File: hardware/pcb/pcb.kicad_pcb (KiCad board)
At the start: 4 copper layers, 41.5 x 66.5 mm, 157 parts, among them J300 Conn_01x02, J301 AudioJack3_Ground_SwitchTR, J400 Conn_02x10_Top_Bottom_Mountin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, J700 USB_B_Micro, U1 AXP209, U101 W25Q32JVZP, U2 SY8008, U300 WM8960, U401 TPS65631W, U402 AP2127K-3.0, U700 USBLC6-2SC6, X100 24.576MHz

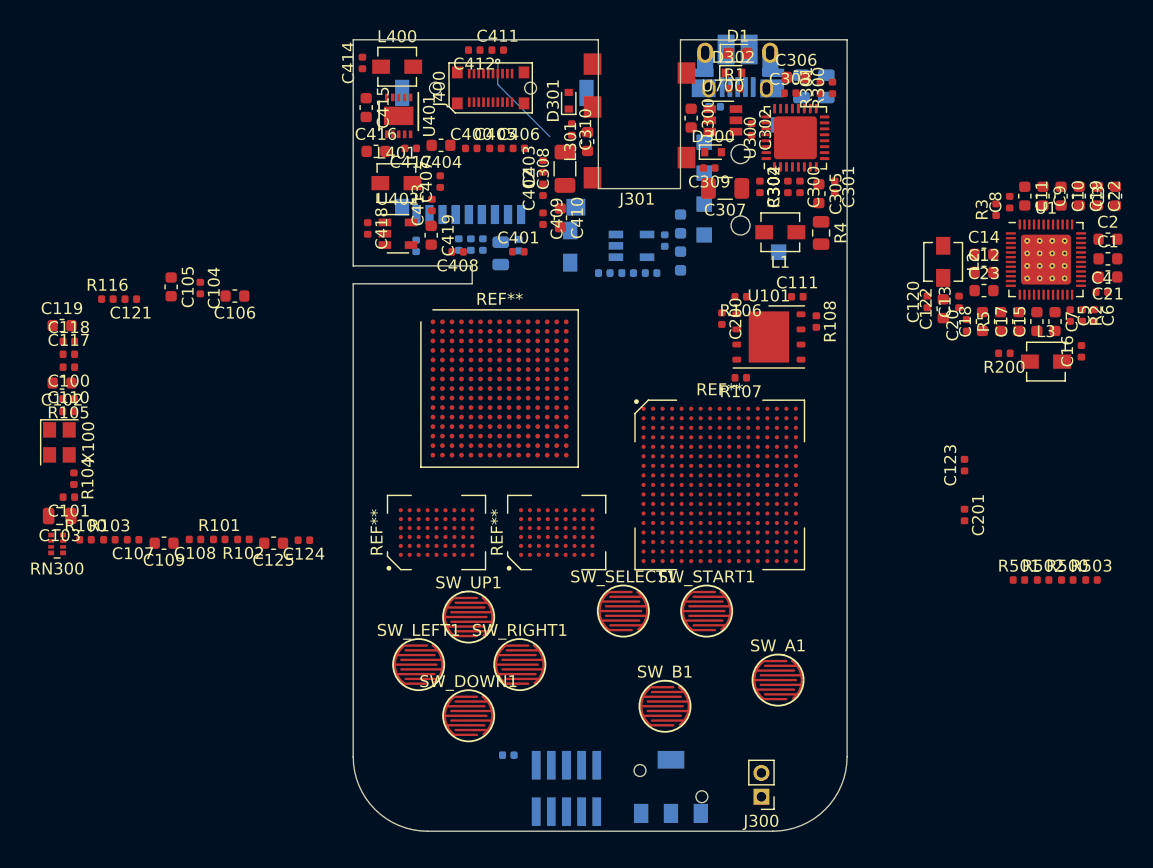
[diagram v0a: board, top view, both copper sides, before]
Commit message: - Migrate to KiCAD 5.99 nightly, pcb initial layout
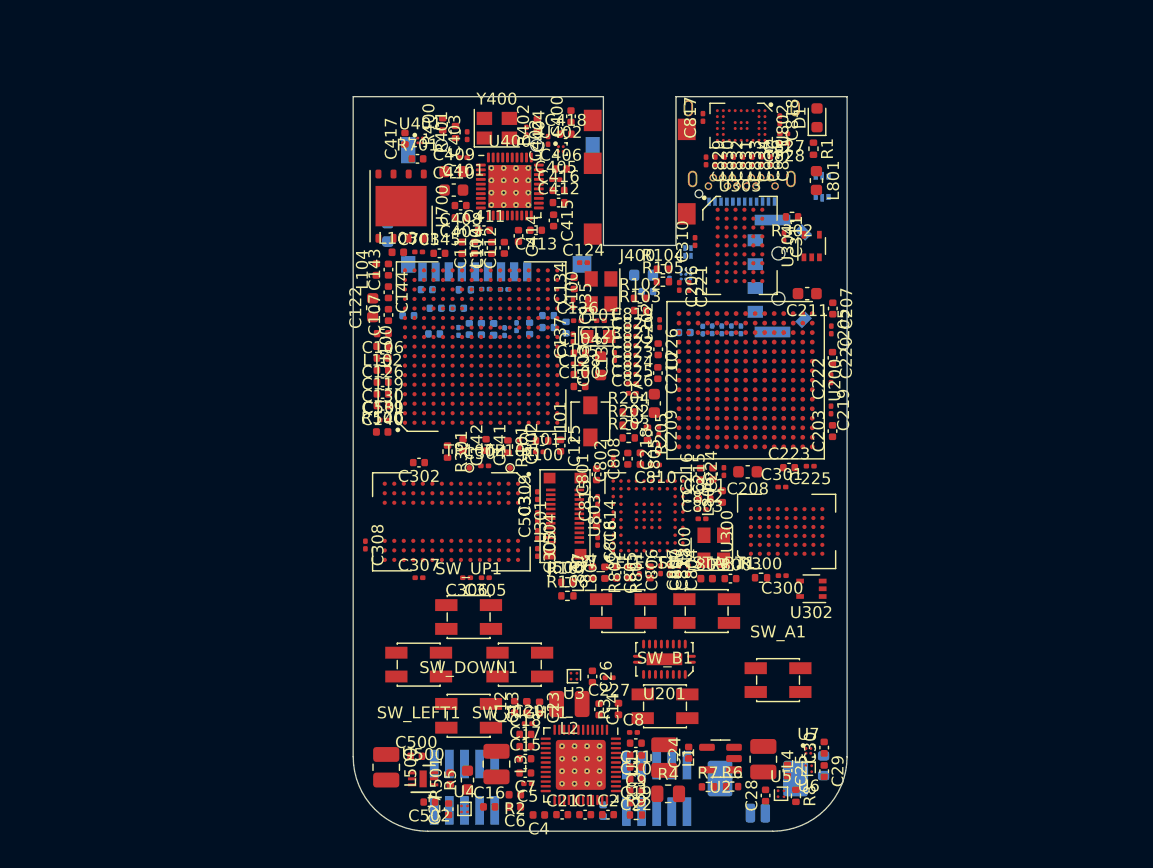
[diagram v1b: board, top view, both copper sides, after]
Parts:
- removed BAT1: Conn_01x03, footprint:BC-15-3P
- removed C419: 4.7uF, Capacitor_SMD:C_0603_1608Metric
- removed C600: 18pF, Capacitor_SMD:C_0402_1005Metric
- removed C601: 47uF, Capacitor_SMD:C_0805_2012Metric
- removed C602: 100nF, Capacitor_SMD:C_0402_1005Metric
- removed D300, D301, D302: ESD5B5.0ST1G, Diode_SMD:D_SOD-523
- removed D700: B72590D0050H160, Diode_SMD:D_0402_1005Metric
- removed ENC1: SIQ-02FVS3, footprint:SIQ-02FVS3
- removed FPGA_JTAG1: Conn_02x05_Odd_Even, Connector_PinHeader_1.27mm:PinHeader_2x05_P1.27mm_Vertical_SMD
- removed J300: Conn_01x02, Connector_PinHeader_2.00mm:PinHeader_1x02_P2.00mm_Vertical
- removed J301: AudioJack3_Ground_SwitchTR, footprint:PJ-327E
- removed J700: USB_B_Micro, Connector_USB:USB_Micro-B_Amphenol_10103594-0001LF_Horizontal
- removed L300, L301: BLM18BD252SN1, Inductor_SMD:L_0603_1608Metric
- removed L400, L401: 10uH, Inductor_SMD:L_Vishay_IHLP-1212
- removed MICRO_SD300: MICRO_SD(TFC-WPAPR-08), footprint:TFC-WPAPR-08
- removed R108: 100K, Capacitor_SMD:C_0402_1005Metric
- removed R116: 2.2K, Capacitor_SMD:C_0402_1005Metric
- removed R117: 4.7K, Capacitor_SMD:C_0402_1005Metric
- removed R502, R503, R601, R602: 10K, Resistor_SMD:R_0402_1005Metric
- removed R600: 33R, Resistor_SMD:R_0402_1005Metric
- removed REF** (x2): BGA-54_6x9_6.0x8.0mm, footprint:BGA-54_6x9_6.0x8.0mm
- removed REF**: BGA-289_17x17_14.0x14.0mm, footprint:BGA-289_17x17_14.0x14.0mm
- removed REF**: Xilinx_CSGA225, Package_BGA:Xilinx_CSGA225
- removed RN300: 22, Resistor_SMD:R_Array_Convex_4x0402
- removed U101: W25Q32JVZP, Package_SON:WSON-8-1EP_6x5mm_P1.27mm_EP3.4x4.3mm
- removed X100: 24.576MHz, Oscillator:Oscillator_SMD_Abracon_ASE-4Pin_3.2x2.5mm
- added BT1: Conn_01x02, Connector_Molex:Molex_PicoBlade_53261-0271_1x02-1MP_P1.25mm_Horizontal, B.Cu at (134.0, 112.6)
- added C112: 1uF, Capacitor_SMD:C_0402_1005Metric, F.Cu at (112.7, 67.5)
- added C113: 2.2uF, Capacitor_SMD:C_0402_1005Metric, F.Cu at (110.2, 67.5)
- added C114: 1uF, Capacitor_SMD:C_0402_1005Metric, F.Cu at (111.6, 67.5)
- added C115: 100nF, Capacitor_SMD:C_0201_0603Metric, B.Cu at (113.7, 74.1)
- added C116: 2.2uF, Capacitor_SMD:C_0402_1005Metric, B.Cu at (114.8, 74.2)
- added C126: 1uF, Capacitor_SMD:C_0402_1005Metric, F.Cu at (102.5, 76.8)
- added C127: 1uF, Capacitor_SMD:C_0402_1005Metric, B.Cu at (106.8, 74.7)
- added C128: 2.2uF, Capacitor_SMD:C_0402_1005Metric, F.Cu at (119.0, 78.1)
- added C129: 2.2uF, Capacitor_SMD:C_0402_1005Metric, B.Cu at (104.6, 73.2)
- added C130: 2.2uF, Capacitor_SMD:C_0402_1005Metric, F.Cu at (102.5, 78.8)
- added C131: 2.2uF, Capacitor_SMD:C_0402_1005Metric, B.Cu at (106.2, 71.0)
- added C132: 2.2uF, Capacitor_SMD:C_0402_1005Metric, B.Cu at (108.8, 72.5)
- added C133: 1uF, Capacitor_SMD:C_0402_1005Metric, B.Cu at (117.9, 74.2)
- added C134: 1uF, Capacitor_SMD:C_0402_1005Metric, F.Cu at (118.6, 70.5)
- added C135: 470nF, Capacitor_SMD:C_0201_0603Metric, F.Cu at (118.5, 72.2)
- added C136: 100nF, Capacitor_SMD:C_0201_0603Metric, F.Cu at (118.8, 73.6)
- added C137: 18pF, Capacitor_SMD:C_0201_0603Metric, F.Cu at (118.5, 75.0)
- added C138: 18pF, Capacitor_SMD:C_0201_0603Metric, F.Cu at (122.0, 76.6)
- added C139: 4.7uF, Capacitor_SMD:C_0402_1005Metric, F.Cu at (102.5, 79.8)
- added C140: 2.2uF, Capacitor_SMD:C_0402_1005Metric, F.Cu at (102.5, 80.8)
- added C141: 4.7uF, Capacitor_SMD:C_0402_1005Metric, F.Cu at (111.2, 84.0)
- added C142: 2.2uF, Capacitor_SMD:C_0402_1005Metric, F.Cu at (109.2, 84.0)
- added C143: 1uF, Capacitor_SMD:C_0402_1005Metric, F.Cu at (103.0, 69.3)
- added C144: 1uF, Capacitor_SMD:C_0402_1005Metric, F.Cu at (103.0, 71.2)
- added C145: 1uF, Capacitor_SMD:C_0402_1005Metric, F.Cu at (107.2, 67.9)
- added C202: 470nF, Capacitor_SMD:C_0201_0603Metric, F.Cu at (125.8, 73.8)
- added C203: 4.7uF, Capacitor_SMD:C_0402_1005Metric, F.Cu at (140.3, 82.9)
- added C204: 4.7uF, Capacitor_SMD:C_0402_1005Metric, B.Cu at (127.8, 74.6)
- added C205: 470nF, Capacitor_SMD:C_0201_0603Metric, F.Cu at (140.2, 74.4)
- added C206: 470nF, Capacitor_SMD:C_0201_0603Metric, F.Cu at (127.4, 70.7)
- added C207: 4.7uF, Capacitor_SMD:C_0402_1005Metric, F.Cu at (140.3, 72.6)
- added C208: 47uF, Capacitor_SMD:C_0603_1608Metric, F.Cu at (133.2, 86.3)
- added C209: 470nF, Capacitor_SMD:C_0201_0603Metric, F.Cu at (125.7, 82.8)
- added C210: 4.7uF, Capacitor_SMD:C_0402_1005Metric, F.Cu at (125.6, 78.0)
- added C211: 47uF, Capacitor_SMD:C_0603_1608Metric, F.Cu at (138.2, 71.3)
- added C212: 470nF, Capacitor_SMD:C_0201_0603Metric, B.Cu at (132.6, 74.4)
- added C213: 470nF, Capacitor_SMD:C_0201_0603Metric, B.Cu at (131.0, 74.4)
- added C214: 470nF, Capacitor_SMD:C_0201_0603Metric, B.Cu at (130.2, 74.4)
- added C215: 4.7uF, Capacitor_SMD:C_0402_1005Metric, F.Cu at (130.2, 86.5)
- added C216: 4.7uF, Capacitor_SMD:C_0402_1005Metric, F.Cu at (129.2, 86.5)
- added C217: 47uF, Capacitor_SMD:C_0603_1608Metric, F.Cu at (125.3, 80.5)
- added C218: 470nF, Capacitor_SMD:C_0201_0603Metric, F.Cu at (125.7, 84.4)
- added C219: 470nF, Capacitor_SMD:C_0201_0603Metric, F.Cu at (140.2, 81.1)
- added C220: 4.7uF, Capacitor_SMD:C_0402_1005Metric, F.Cu at (140.3, 76.7)
- added C221: 470nF, Capacitor_SMD:C_0201_0603Metric, F.Cu at (128.2, 70.7)
- added C222: 470nF, Capacitor_SMD:C_0201_0603Metric, F.Cu at (140.2, 78.5)
- added C223: 4.7uF, Capacitor_SMD:C_0402_1005Metric, F.Cu at (136.6, 86.0)
- added C224: 470nF, Capacitor_SMD:C_0201_0603Metric, F.Cu at (131.2, 86.3)
- added C225: 470nF, Capacitor_SMD:C_0201_0603Metric, F.Cu at (138.4, 85.8)
- added C226: 4.7uF, Capacitor_SMD:C_0402_1005Metric, F.Cu at (125.6, 76.0)
- added C227: 100nF, Capacitor_SMD:C_0201_0603Metric, F.Cu at (121.5, 103.6)
- added C26: 1uF, Capacitor_SMD:C_0402_1005Metric, F.Cu at (120.1, 103.5)
- added C27: 1uF, Capacitor_SMD:C_0402_1005Metric, F.Cu at (108.0, 114.7)
- added C28: 1uF, Capacitor_SMD:C_0402_1005Metric, F.Cu at (134.7, 113.5)
- added C29: 1uF, Capacitor_SMD:C_0402_1005Metric, F.Cu at (139.6, 111.5)
- added C30: 1uF, Capacitor_SMD:C_0402_1005Metric, F.Cu at (139.6, 109.5)
- added C311: 470nF, Capacitor_SMD:C_0201_0603Metric, F.Cu at (136.2, 66.5)
- added C500: 1uF, Capacitor_SMD:C_0402_1005Metric, F.Cu at (105.3, 110.2)
- added C501: 100nF, Capacitor_SMD:C_0201_0603Metric, F.Cu at (102.5, 82.0)
- added C502: 1uF, Capacitor_SMD:C_0402_1005Metric, F.Cu at (106.4, 114.0)
- added C503: 470nF, Capacitor_SMD:C_0201_0603Metric, F.Cu at (115.5, 90.1)
- added C504: 470nF, Capacitor_SMD:C_0201_0603Metric, F.Cu at (115.5, 91.6)
- added C702: 100nF, Capacitor_SMD:C_0201_0603Metric, B.Cu at (112.7, 71.0)
- added C703: 470nF, Capacitor_SMD:C_0201_0603Metric, F.Cu at (105.5, 67.8)
- added C800: 470nF, Capacitor_SMD:C_0201_0603Metric, F.Cu at (128.2, 94.5)
- added C801: 1uF, Capacitor_SMD:C_0402_1005Metric, F.Cu at (120.5, 86.5)
- added C802: 100nF, Capacitor_SMD:C_0201_0603Metric, F.Cu at (121.8, 85.4)
- added C803: 100nF, Capacitor_SMD:C_0201_0603Metric, F.Cu at (129.3, 90.2)
- added C804: 100nF, Capacitor_SMD:C_0201_0603Metric, F.Cu at (127.4, 94.5)
- added C805: 1uF, Capacitor_SMD:C_0402_1005Metric, F.Cu at (122.1, 94.8)
- added C806: 100nF, Capacitor_SMD:C_0201_0603Metric, F.Cu at (124.0, 94.5)
- added C807: 100nF, Capacitor_SMD:C_0201_0603Metric, F.Cu at (125.8, 94.5)
- added C808: 1uF, Capacitor_SMD:C_0402_1005Metric, F.Cu at (123.1, 85.2)
- added C810: 100nF, Capacitor_SMD:C_0201_0603Metric, F.Cu at (125.4, 85.7)
- added C811: 1uF, Capacitor_SMD:C_0402_1005Metric, F.Cu at (129.5, 88.6)
- added C812: 100nF, Capacitor_SMD:C_0201_0603Metric, F.Cu at (129.3, 89.5)
- added C813: 100nF, Capacitor_SMD:C_0201_0603Metric, F.Cu at (126.6, 94.5)
- added C814: 1uF, Capacitor_SMD:C_0402_1005Metric, F.Cu at (120.4, 90.4)
- added C815: 100nF, Capacitor_SMD:C_0201_0603Metric, F.Cu at (120.5, 88.7)
- added C816: 100nF, Capacitor_SMD:C_0201_0603Metric, F.Cu at (120.5, 92.1)
- added C817: 100nF, Capacitor_SMD:C_0201_0603Metric, F.Cu at (129.4, 56.5)
- added C818: 100nF, Capacitor_SMD:C_0201_0603Metric, F.Cu at (135.8, 56.7)
- added C819: 100nF, Capacitor_SMD:C_0201_0603Metric, F.Cu at (123.4, 74.1)
- added C820: 100nF, Capacitor_SMD:C_0201_0603Metric, F.Cu at (123.4, 74.9)
- added C821: 100nF, Capacitor_SMD:C_0201_0603Metric, F.Cu at (123.4, 75.7)
- added C822: 100nF, Capacitor_SMD:C_0201_0603Metric, F.Cu at (123.4, 76.5)
- added C823: 100nF, Capacitor_SMD:C_0201_0603Metric, F.Cu at (123.4, 77.3)
- added C824: 100nF, Capacitor_SMD:C_0201_0603Metric, F.Cu at (123.4, 78.1)
- added C825: 100nF, Capacitor_SMD:C_0201_0603Metric, F.Cu at (123.4, 78.9)
- added C826: 100nF, Capacitor_SMD:C_0201_0603Metric, F.Cu at (123.4, 79.7)
- added C827: 100nF, Capacitor_SMD:C_0201_0603Metric, F.Cu at (136.2, 57.9)
- added C828: 100nF, Capacitor_SMD:C_0201_0603Metric, F.Cu at (136.2, 58.7)
- added C829: 100nF, Capacitor_SMD:C_0201_0603Metric, F.Cu at (129.7, 60.2)
- added C830: 100nF, Capacitor_SMD:C_0201_0603Metric, F.Cu at (130.4, 60.2)
- added C831: 100nF, Capacitor_SMD:C_0201_0603Metric, F.Cu at (132.0, 60.2)
- added C832: 100nF, Capacitor_SMD:C_0201_0603Metric, F.Cu at (131.2, 60.2)
- added C833: 100nF, Capacitor_SMD:C_0201_0603Metric, F.Cu at (132.8, 60.2)
- added C834: 100nF, Capacitor_SMD:C_0201_0603Metric, F.Cu at (133.5, 60.2)
- added C835: 100nF, Capacitor_SMD:C_0201_0603Metric, F.Cu at (135.1, 60.1)
- added C836: 100nF, Capacitor_SMD:C_0201_0603Metric, F.Cu at (134.3, 60.1)
- added C837: 10uF, Capacitor_SMD:C_0402_1005Metric, B.Cu at (124.7, 71.2)
- added C838: 100nF, Capacitor_SMD:C_0201_0603Metric, B.Cu at (126.6, 69.7)
- added J100: Conn_02x05_Odd_Even, Connector_PinHeader_1.27mm:PinHeader_2x05_P1.27mm_Vertical_SMD, B.Cu at (109.3, 112.8)
- added J200: Conn_02x05_Odd_Even, Connector_PinHeader_1.27mm:PinHeader_2x05_P1.27mm_Vertical_SMD, B.Cu at (125.5, 112.9)
- added J500: AXT524124, footprint:AXT524124, F.Cu at (117.8, 90.0)
- added J800: USB_C_Receptacle, Connector_USB:USB_C_Receptacle_Amphenol_12401548E4-2A, B.Cu at (132.7, 58.6)
- added L100: 120R, Inductor_SMD:L_0402_1005Metric, F.Cu at (109.2, 67.5)
- added L101: LQH3NPN4R7MGRL, Inductor_SMD:L_Vishay_IHLP-1212, F.Cu at (119.9, 82.1)
- added L102: 120R, Inductor_SMD:L_0402_1005Metric, F.Cu at (102.5, 75.8)
- added L103: 120R, Inductor_SMD:L_0402_1005Metric, F.Cu at (103.8, 67.8)
- added L104: 120R, Inductor_SMD:L_0402_1005Metric, F.Cu at (101.9, 69.3)
- added L500: LQH2HPN100MGRL, Inductor_SMD:L_1008_2520Metric, F.Cu at (102.8, 111.1)
- added L800: EXC14CE900U, footprint:L_CommonModeChoke_Panasonic_EXC14CE, B.Cu at (128.1, 67.8)
- added L801: 300R, Inductor_SMD:L_0603_1608Metric, F.Cu at (138.9, 61.8)
- added L802: 300R, Inductor_SMD:L_0603_1608Metric, B.Cu at (124.4, 69.8)
- added L803: 120R, Inductor_SMD:L_0402_1005Metric, F.Cu at (129.7, 95.3)
- added L804: 120R, Inductor_SMD:L_0402_1005Metric, F.Cu at (121.2, 94.8)
- added L805: 120R, Inductor_SMD:L_0402_1005Metric, F.Cu at (124.1, 85.2)
- added L806: 120R, Inductor_SMD:L_0402_1005Metric, F.Cu at (131.0, 88.4)
- added L807: 120R, Inductor_SMD:L_0402_1005Metric, F.Cu at (120.1, 94.8)
- added MICRO_SD700: MICRO_SD(TFC-WPAPR-08), footprint:TFC-WPAPR-08, B.Cu at (112.4, 62.1)
- added R202: 10K, Resistor_SMD:R_0402_1005Metric, F.Cu at (123.1, 82.4)
- added R203: 10K, Resistor_SMD:R_0402_1005Metric, F.Cu at (123.2, 83.5)
- added R204: 10K, Resistor_SMD:R_0402_1005Metric, F.Cu at (123.2, 81.3)
- added R205: 2.2K, Resistor_SMD:R_0402_1005Metric, F.Cu at (124.7, 83.1)
- added R400: 33, Resistor_SMD:R_0402_1005Metric, F.Cu at (107.5, 57.1)
- added R401: 33, Resistor_SMD:R_0402_1005Metric, F.Cu at (108.6, 57.8)
- added R402: 33, Resistor_SMD:R_0402_1005Metric, F.Cu at (115.5, 57.2)
- added R8: 100K, Resistor_SMD:R_0402_1005Metric, F.Cu at (137.2, 113.5)
- added R800: 10K, Capacitor_SMD:C_0402_1005Metric, F.Cu at (131.7, 95.3)
- added R801: 3K/1%, Capacitor_SMD:C_0402_1005Metric, F.Cu at (125.0, 94.8)
- added R802: 10K, Capacitor_SMD:C_0402_1005Metric, F.Cu at (123.2, 94.8)
- added R9: 100K, Resistor_SMD:R_0402_1005Metric, F.Cu at (123.8, 115.1)
- added SW600: K1-1511SA-02, footprint:K1-1511SA-02, B.Cu at (134.7, 69.8)
- added TH1: 100K, Resistor_SMD:R_0603_1608Metric, B.Cu at (139.5, 111.0)
- added TP100: TestPoint, footprint:TestPoint_Pad_D0.5mm, F.Cu at (109.8, 86.0)
- added TP101: TestPoint, footprint:TestPoint_Pad_D0.5mm, F.Cu at (113.2, 86.0)
- added U100: MIMXRT1176DVMAA, footprint:BGA-289_17x17_14.0x14.0mm, F.Cu at (110.8, 75.8)
- added U200: XC7S25-CSGA225, Package_BGA:Xilinx_CSGA225, F.Cu at (133.0, 78.6)
- added U201: 74LVCH245A, footprint:DHVQFN-20_EP_4.5x2.5_Pitch0.5mm, F.Cu at (126.2, 102.0)
- added U3: NX3P1108UK, Package_CSP:WLCSP-4-X1-WLB0909-4_0.89x0.89mm_P0.5mm, F.Cu at (118.5, 103.5)
- added U301: MT48H16M32LFB5-6 or IS42VM32160E-6 or W989D2DBJX6, footprint:BGA-90_9x15_8.0x13.0mm, F.Cu at (108.2, 90.5)
- added U302: 74LVC1G126, Package_TO_SOT_SMD:SOT-353_SC-70-5, F.Cu at (138.5, 96.1)
- added U303: IS66WVC4M16-ALL, footprint:BGA-54_6x9_6.0x8.0mm, F.Cu at (132.5, 67.3)
- added U304: 74LVC1G126, Package_TO_SOT_SMD:SOT-353_SC-70-5, F.Cu at (138.5, 67.3)
- added U4: NX3P1108UK, Package_CSP:WLCSP-4-X1-WLB0909-4_0.89x0.89mm_P0.5mm, F.Cu at (109.3, 114.6)
- added U400: CS43130, Package_DFN_QFN:QFN-40-1EP_5x5mm_P0.4mm_EP3.6x3.6mm_ThermalVias, F.Cu at (113.2, 62.3)
- added U5: NX3P1108UK, Package_CSP:WLCSP-4-X1-WLB0909-4_0.89x0.89mm_P0.5mm, F.Cu at (135.9, 113.3)
- added U500: LT3491, Package_DFN_QFN:DFN-6-1EP_2x2mm_P0.5mm_EP0.61x1.42mm, F.Cu at (105.9, 112.1)
- added U6: NX3P1108UK, Package_CSP:WLCSP-4-X1-WLB0909-4_0.89x0.89mm_P0.5mm, F.Cu at (138.3, 111.2)
- added U7: ADP121-1.2, footprint:CSP-4_2x2_0.8x0.8mm, F.Cu at (138.2, 109.8)
- added U800: USBLC6-2P6, Package_TO_SOT_SMD:SOT-666, B.Cu at (139.4, 62.4)
- added U801: FUSB302UCX, Package_BGA:WLP-9_1.448x1.468mm_Layout3x3_P0.4mm_Ball0.27mm_Pad0.25mm, B.Cu at (128.0, 69.7)
- added U802: CBTL08GP053, footprint:BGA-40_6x9_3.5x5.0mm, F.Cu at (132.6, 57.2)
- added U803: TC358777, footprint:BGA-80_10x10_7.0x7.0mm, F.Cu at (124.8, 90.0)
- added X800: 19.2MHz, Oscillator:Oscillator_SMD_Abracon_ASE-4Pin_3.2x2.5mm, F.Cu at (130.3, 92.7)
- added Y100: 24MHz, Oscillator:Oscillator_SMD_Abracon_ASE-4Pin_3.2x2.5mm, F.Cu at (120.8, 71.1)
- added Y101: 32.768K, Crystal:Crystal_SMD_TXC_9HT11-2Pin_2.0x1.2mm_HandSoldering, F.Cu at (120.6, 74.9)
- added Y400: 22.5792MHz, Oscillator:Oscillator_SMD_Abracon_ASE-4Pin_3.2x2.5mm, F.Cu at (112.1, 57.4)
- C1, C10, C11, C12, C14, C15, C17, C18, C19, C2, C21, C22, C23, C3, C7, C9: footprint Capacitor_SMD:C_0603_1608Metric -> Capacitor_SMD:C_0402_1005Metric
- C100, C406: value 470nF -> 4.7uF
- C101, C20, C300, C301, C309, C8: footprint Capacitor_SMD:C_0402_1005Metric -> Capacitor_SMD:C_0201_0603Metric
- C102, C105, C305, C306: value 4.7uF -> 100nF; footprint Capacitor_SMD:C_0603_1608Metric -> Capacitor_SMD:C_0201_0603Metric
- C103: value 47uF -> 22uF; footprint Capacitor_SMD:C_0805_2012Metric -> Capacitor_SMD:C_0603_1608Metric
- C104, C107, C407, C408, C411, C412, C413, C414: value 470nF -> 2.2uF
- C106: value 4.7uF -> 10uF; footprint Capacitor_SMD:C_0603_1608Metric -> Capacitor_SMD:C_0402_1005Metric
- C108, C117: value 470nF -> 100nF; footprint Capacitor_SMD:C_0402_1005Metric -> Capacitor_SMD:C_0201_0603Metric; moved to B.Cu
- C109: footprint Capacitor_SMD:C_0603_1608Metric -> Capacitor_SMD:C_0402_1005Metric; moved to B.Cu
- C110, C120, C121: value 470nF -> 4.7uF; moved to B.Cu
- C111: value 470nF -> 2.2uF; moved to B.Cu
- C118: value 470nF -> 1uF; moved to B.Cu
- C119: value 4.7uF -> 1uF; footprint Capacitor_SMD:C_0603_1608Metric -> Capacitor_SMD:C_0402_1005Metric
- C122: value 4.7uF -> 47uF
- C123, C124, C403: value 470nF -> 18pF; footprint Capacitor_SMD:C_0402_1005Metric -> Capacitor_SMD:C_0201_0603Metric
- C125: value 4.7uF -> 2.2uF; footprint Capacitor_SMD:C_0603_1608Metric -> Capacitor_SMD:C_0402_1005Metric
- C200, C201: footprint Capacitor_SMD:C_0402_1005Metric -> Capacitor_SMD:C_0201_0603Metric; moved to B.Cu
- C24, C25: value 470nF -> 10uF; moved to F.Cu
- C302, C400: value 470nF -> 10uF
- C303, C304, C401, C402, C405: value 470nF -> 100nF; footprint Capacitor_SMD:C_0402_1005Metric -> Capacitor_SMD:C_0201_0603Metric
- C307, C308: value 100uF -> 100nF; footprint Capacitor_SMD:C_1206_3216Metric -> Capacitor_SMD:C_0201_0603Metric
- C310: value 100nF -> 470nF; footprint Capacitor_SMD:C_0402_1005Metric -> Capacitor_SMD:C_0201_0603Metric
- C404: value 4.7uF -> 18pF; footprint Capacitor_SMD:C_0603_1608Metric -> Capacitor_SMD:C_0201_0603Metric
- C409: value 470nF -> 15uF; footprint Capacitor_SMD:C_0402_1005Metric -> Capacitor_SMD:C_0603_1608Metric
- C410: value 4.7uF -> 15uF
- C415, C416: value 10uF -> 2.2uF; footprint Capacitor_SMD:C_0603_1608Metric -> Capacitor_SMD:C_0402_1005Metric
- C417, C418: value 470nF -> 1uF
- C5: value 220nF -> 470nF; footprint Capacitor_SMD:C_0402_1005Metric -> Capacitor_SMD:C_0201_0603Metric
- C700: value 10uF -> 18pF/DNP; footprint Capacitor_SMD:C_0603_1608Metric -> Capacitor_SMD:C_0201_0603Metric
- C701: value 100nF -> 22uF; footprint Capacitor_SMD:C_0805_2012Metric -> Capacitor_SMD:C_0603_1608Metric
- J400: value Conn_02x10_Top_Bottom_MountingPin -> AudioJack3_SwitchT; footprint footprint:AXE520124 -> footprint:PJ-327E
- L1, L2, L3: footprint Inductor_SMD:L_Vishay_IHLP-1212 -> Inductor_SMD:L_1008_2520Metric
- L4: value 2.2uH -> 4.7uH; footprint Inductor_SMD:L_Vishay_IHLP-1212 -> Inductor_SMD:L_1008_2520Metric; moved to F.Cu
- R100: value 10K -> 30K; footprint Capacitor_SMD:C_0402_1005Metric -> Resistor_SMD:R_0402_1005Metric
- R101, R103, R105: value 10K -> 4.7K; footprint Capacitor_SMD:C_0402_1005Metric -> Resistor_SMD:R_0402_1005Metric
- R102: value 1K -> 4.7K; footprint Capacitor_SMD:C_0402_1005Metric -> Resistor_SMD:R_0402_1005Metric
- R104: value 33R -> 4.7K; footprint Capacitor_SMD:C_0402_1005Metric -> Resistor_SMD:R_0402_1005Metric
- R106, R107: value 100K -> 4.7K; footprint Capacitor_SMD:C_0402_1005Metric -> Resistor_SMD:R_0402_1005Metric
- R200: value 10K -> 4.7K; moved to B.Cu
- R300: value 22R -> 10K
- R301: value 22R -> 0
- R302: value 47K -> 10K
- R500: value 10K -> 100K
- R501: value 10K -> 127
- R6: value 20K -> 200K; moved to F.Cu
- R7: value 10K -> 100K; moved to F.Cu
- R700: value 1R -> 0; footprint Resistor_SMD:R_0603_1608Metric -> Resistor_SMD:R_0402_1005Metric
- R701: value 0 -> 100K; footprint Resistor_SMD:R_0805_2012Metric -> Capacitor_SMD:C_0402_1005Metric; moved to F.Cu
- SW_A1, SW_B1, SW_DOWN1, SW_LEFT1, SW_RIGHT1, SW_SELECT1, SW_START1, SW_UP1: footprint footprint:Contact_4mm -> footprint:SW_SPST_K21177SR
- U2: moved to F.Cu
- U300: value WM8960 -> IS66WVC4M16-ALL; footprint Package_DFN_QFN:QFN-32-1EP_5x5mm_P0.5mm_EP3.6x3.6mm -> footprint:BGA-54_6x9_6.0x8.0mm
- U401: value TPS65631W -> ADP150-1.8; footprint Package_DFN_QFN:DFN-10-1EP_3x3mm_P0.5mm_EP1.55x2.48mm -> footprint:CSP-4_2x2_0.8x0.8mm
- U402: value AP2127K-3.0 -> ADP150-1.8; footprint Package_TO_SOT_SMD:SOT-23-5 -> footprint:CSP-4_2x2_0.8x0.8mm
- U700: value USBLC6-2SC6 -> W25Q128JVP; footprint Package_TO_SOT_SMD:SOT-23-6 -> Package_SON:WSON-8-1EP_6x5mm_P1.27mm_EP3.4x4.3mm
- moved C3 65.0 mm to (123.8, 114.1), turned to 0 degrees
- moved C4 64.6 mm to (115.6, 115.1), turned to 180 degrees
- moved C21 64.4 mm to (117.6, 115.1), turned to 0 degrees
- moved C1 64.1 mm to (119.5, 115.1)
- moved C2 64.1 mm to (121.4, 115.1)
- moved C6 63.8 mm to (113.6, 114.5), turned to 180 degrees
- moved C22 63.3 mm to (123.8, 113.1), turned to 180 degrees
- moved C16 62.8 mm to (111.4, 114.5), turned to 0 degrees
- moved R2 62.4 mm to (113.6, 113.4), turned to 180 degrees
- moved C19 61.5 mm to (123.8, 112.1), turned to 180 degrees
- moved C5 60.2 mm to (114.7, 112.5), turned to 180 degrees
- moved R5 59.1 mm to (109.6, 112.2)
- moved C10 59.0 mm to (123.8, 110.1), turned to 180 degrees
- moved C9 58.9 mm to (123.8, 111.1), turned to 180 degrees
- moved R500 58.9 mm to (102.4, 83.0)
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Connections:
- C100 pad 1: +3V3 -> IPSOUT
- C101 pad 1: +3V3 -> Net-(C101-Pad1)
- C102 pad 1: +3V3 -> Net-(C102-Pad1)
- C103 pad 1: +3V3 -> +1V8A
- C104 pad 1: GND -> +1V8A
- C104 pad 2: +1V2 -> GND
- C105 pad 1: GND -> +1V8A
- C105 pad 2: +1V2 -> GND
- C106 pad 1: GND -> /mcu/VDD_SOC
- C106 pad 2: +1V2 -> GND
- C107 pad 1: +3V3 -> /mcu/VDD_SOC
- C108 pad 1: +3V3 -> /mcu/VDD_SOC
- C110 pad 1: GND -> Net-(C110-Pad1)
- C110 pad 2: +3V3 -> GND
- C111 pad 1: GND -> Net-(C111-Pad1)
- C111 pad 2: Net-(C111-Pad2) -> GND
- C117 pad 1: GND -> /mcu/VDD_SOC
- C117 pad 2: +3V3 -> GND
- C118 pad 1: GND -> /mcu/VDD_SOC
- C118 pad 2: +3V3 -> GND
- C119 pad 1: GND -> /mcu/VDD_SOC
- C119 pad 2: +3V3 -> GND
- C12 pad 2: +1V2 -> Net-(C12-Pad2)
- C120 pad 1: +1V8 -> /mcu/VDD_SOC
- C121 pad 1: +1V8 -> /mcu/VDD_SOC
- C122 pad 1: +1V8 -> /mcu/VDD_SOC
- C123 pad 1: GND -> Net-(C123-Pad1)
- C123 pad 2: +1V8 -> GND
- C124 pad 1: GND -> Net-(C124-Pad1)
- C124 pad 2: +1V8 -> GND
- C125 pad 1: GND -> +1V8
- C125 pad 2: +1V8 -> GND
- C13 pad 2: +1V2 -> Net-(C12-Pad2)
- C200 pad 1: +RAM -> GND
- C200 pad 2: GND -> +1V8_FPGA
- C201 pad 1: +RAM -> GND
- C201 pad 2: GND -> +1V8_FPGA
- C300 pad 1: +1V8 -> +RAM
- C301 pad 1: +1V8 -> +RAM
- C302 pad 1: +3V3 -> +1V8
- C303 pad 1: +3V3 -> +1V8
- C304 pad 1: +3.3VA -> +1V8
- C305 pad 1: +3.3VA -> +1V8
- C306 pad 1: +3V3 -> +1V8
- C307 pad 1: Net-(C307-Pad1) -> +1V8
- C307 pad 2: Net-(C307-Pad2) -> GND
- C308 pad 1: Net-(C308-Pad1) -> +1V8
- C308 pad 2: Net-(C308-Pad2) -> GND
- C309 pad 1: GND -> +1V8
- C309 pad 2: Net-(C307-Pad2) -> GND
- C310 pad 1: GND -> +RAM
- C310 pad 2: Net-(C308-Pad2) -> GND
- C400 pad 1: +1V8 -> +1V8A
- C401 pad 1: +1V8 -> +1V8A
- C402 pad 1: +1V8 -> +1V8A
- C403 pad 1: +1V8 -> Net-(C403-Pad1)
- C404 pad 1: +1V8 -> Net-(C404-Pad1)
- C405 pad 1: +1V2 -> +3.3VA
- C406 pad 1: +1V2 -> +3.3VA
- C407 pad 1: +1V2 -> Net-(C407-Pad1)
- C408 pad 1: +1V2 -> Net-(C408-Pad1)
- C409 pad 1: +1V2 -> Net-(C408-Pad1)
- C409 pad 2: GND -> Net-(C409-Pad2)
- C410 pad 1: +1V2 -> Net-(C407-Pad1)
- C410 pad 2: GND -> Net-(C410-Pad2)
- C411 pad 1: +1V8 -> Net-(C411-Pad1)
- C411 pad 2: GND -> Net-(C411-Pad2)
- C412 pad 1: +3V0 -> Net-(C412-Pad1)
- C412 pad 2: GND -> Net-(C412-Pad2)
- C413 pad 1: GND -> Net-(C412-Pad1)
- C413 pad 2: +3V3 -> Net-(C413-Pad2)
- C414 pad 1: +3V3 -> Net-(C414-Pad1)
- C416 pad 1: GND -> Net-(C416-Pad1)
- C416 pad 2: /lcd/ELVSS -> GND
- C417 pad 1: GND -> +3V3
- C417 pad 2: +3V3 -> GND
- C700 pad 1: VBUS -> Net-(C700-Pad1)
- C700 pad 2: Net-(C700-Pad2) -> GND
- C701 pad 1: Net-(C701-Pad1) -> +3V3
- L2 pad 2: +1V2 -> Net-(C12-Pad2)
- R100 pad 1: +3V3 -> IPSOUT
- R100 pad 2: (no net) -> Net-(C101-Pad1)
- R101 pad 1: +3V3 -> Net-(C102-Pad1)
- R101 pad 2: (no net) -> GND
- R102 pad 1: GND -> +1V8
- R102 pad 2: (no net) -> I2C1_SCL
- R103 pad 1: +3V3 -> +1V8
- R103 pad 2: (no net) -> I2C1_SDA
- R104 pad 1: /syscon/GCLK -> +3V3
- R104 pad 2: (no net) -> I2C3_SCL
- R105 pad 2: Net-(R105-Pad2) -> I2C3_SDA
- R106 pad 1: Net-(C111-Pad2) -> +1V8_DP
- R106 pad 2: /syscon/FPGA_CS_N -> I2C4_SDA
- R107 pad 1: Net-(C111-Pad2) -> +1V8_DP
- R107 pad 2: Net-(R107-Pad2) -> I2C4_SCL
- R200 pad 1: +RAM -> +1V8_FPGA
- R200 pad 2: /ram/RAM_CE_N -> /fpga/FPGA_TCK
- R300 pad 1: Net-(R300-Pad1) -> +RAM
- R300 pad 2: (no net) -> Net-(R300-Pad2)
- R301 pad 1: Net-(R301-Pad1) -> SDRAM_CLK
- R301 pad 2: (no net) -> Net-(R301-Pad2)
- R302 pad 1: +3.3VA -> +RAM
- R302 pad 2: Net-(D302-Pad1) -> Net-(R302-Pad2)
- R500 pad 1: +3V3 -> Net-(C501-Pad1)
- R500 pad 2: P13 -> LCD_BL_PWM
- R501 pad 1: +3V3 -> Net-(C502-Pad1)
- R501 pad 2: P12 -> /lcd/LEDA
- R700 pad 1: Net-(C700-Pad2) -> Net-(C700-Pad1)
- R700 pad 2: GND -> SD_CLK
- R701 pad 1: Net-(C701-Pad1) -> +3V3
- R701 pad 2: GND -> FSPI_1A_CS
- SW_A1 pad 1: P15 -> KEY_A
- SW_A1 pad 2: P10 -> GND
- SW_B1 pad 1: P15 -> KEY_B
- SW_B1 pad 2: P11 -> GND
- SW_DOWN1 pad 1: P14 -> KEY_DOWN
- SW_DOWN1 pad 2: P13 -> GND
- SW_LEFT1 pad 1: P14 -> KEY_LEFT
- SW_LEFT1 pad 2: P11 -> GND
- SW_RIGHT1 pad 1: P14 -> KEY_RIGHT
- SW_RIGHT1 pad 2: P10 -> GND
- SW_SELECT1 pad 1: P15 -> KEY_SELECT
- SW_SELECT1 pad 2: P12 -> GND
- SW_START1 pad 1: P15 -> KEY_START
- SW_START1 pad 2: P13 -> GND
- SW_UP1 pad 1: P14 -> KEY_UP
- SW_UP1 pad 2: P12 -> GND
- U1 pad 1: (no net) -> I2C3_SDA
- U1 pad 10: +1V2 -> Net-(C12-Pad2)
- U1 pad 18: (no net) -> WAKEUP
- U1 pad 2: (no net) -> I2C3_SCL
- U1 pad 25: (no net) -> PWROK
- U1 pad 3: (no net) -> unconnected-(U1-Pad3)
- U1 pad 30: (no net) -> unconnected-(U1-Pad30)
- U1 pad 32: (no net) -> unconnected-(U1-Pad32)
- U1 pad 33: (no net) -> unconnected-(U1-Pad33)
- U1 pad 48: (no net) -> PMU_IRQ
- U1 pad 5: (no net) -> unconnected-(U1-Pad5)
- U1 pad 6: (no net) -> PMU_VBUSEN
- U2 pad 1: EXTEN -> FPGA_PWR_EN
- U700 pad 1: USB_DM -> FSPI_1A_CS
- U700 pad 2: GND -> FSPI_1A_D1
- U700 pad 3: USB_DP -> FSPI_1A_D2
- U700 pad 4: USB_DP -> GND
- U700 pad 5: (no net) -> FSPI_1A_D0
- U700 pad 6: USB_DM -> FSPI_1A_SCK
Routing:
- net (no net): track 9.19 -> 0.00 mm, vias 1 -> 0
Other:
- board size 41.5 x 66.5 mm -> 41.5 x 61.7 mm
- net class Default removed
- net class MIPI removed

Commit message: - Working on pcb layout
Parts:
- removed C823, C824, C825, C826, C829, C830, C831, C832, C833, C834, C835, C836: 100nF, Capacitor_SMD:C_0201_0603Metric
- removed J100: Conn_02x05_Odd_Even, Connector_PinHeader_1.27mm:PinHeader_2x05_P1.27mm_Vertical_SMD
- added C146: 100nF, Capacitor_SMD:C_0201_0603Metric, F.Cu at (136.0, 96.0)
- added J101: Conn_01x04, Connector_PinHeader_1.27mm:PinHeader_1x04_P1.27mm_Vertical_SMD_Pin1Left, B.Cu at (126.2, 113.0)
- added U8: PCA9555AHF, Package_DFN_QFN:HVQFN-24-1EP_4x4mm_P0.5mm_EP2.5x2.5mm, F.Cu at (135.4, 99.1)
- C212, C838, U801: moved to F.Cu
- moved R104 27.7 mm to (116.8, 95.4)
- moved R103 26.4 mm to (102.5, 57.6)
- moved R102 26.4 mm to (102.5, 56.6)
- moved R105 25.7 mm to (116.8, 94.4)
- moved C821 22.3 mm to (135.7, 57.0), turned to 180 degrees
- moved C822 22.3 mm to (135.7, 57.8), turned to 180 degrees
- moved C820 20.4 mm to (131.0, 56.0), turned to -90 degrees
- moved C819 20.0 mm to (131.8, 56.0), turned to -90 degrees
- moved C837 19.4 mm to (140.1, 59.2), turned to 90 degrees
- moved L802 17.8 mm to (140.3, 61.8), turned to -90 degrees
- moved C838 16.8 mm to (138.1, 57.5), turned to 180 degrees
- moved U800 15.8 mm to (124.8, 68.4), turned to 0 degrees
- moved J200 14.9 mm to (110.6, 113.0)
- moved R200 14.9 mm to (106.2, 113.0), turned to -90 degrees
- moved U801 14.8 mm to (138.1, 58.9), turned to 0 degrees
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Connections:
- C817 pad 1: +1V8 -> +3V3
- R400 pad 2: SAI4_TX_DATA -> SAI1_RX_SYNC
- R401 pad 2: SAI4_TX_SYNC -> SAI1_RX_BCLK
- R402 pad 2: SAI4_TX_BCLK -> SAI1_RX_DATA0
- U1 pad 6: PMU_VBUSEN -> unconnected-(U1-Pad6)
- U100 pad R5: /mcu/JTAG_TRSTB -> unconnected-(U100-PadR5)
- U100 pad T5: /mcu/JTAG_TDO -> unconnected-(U100-PadT5)
- U100 pad U5: /mcu/JTAG_TDI -> unconnected-(U100-PadU5)
- U200 pad A10: CRAMA_OEN -> CRAMA_A17
- U200 pad A11: CRAMA_CRE -> CRAMA_A15
- U200 pad A12: CRAMA_WAIT -> CRAMA_A13
- U200 pad A14: CRAMA_ADVN -> CRAMA_WAIT
- U200 pad A2: CRAMB_DQ4 -> CRAMB_DQ1
- U200 pad A3: CRAMB_DQ2 -> CRAMB_DQ3
- U200 pad A4: CRAMB_DQ1 -> CRAMB_DQ4
- U200 pad A5: CRAMA_DQ9 -> CRAMA_A20
- U200 pad A6: CRAMA_DQ10 -> CRAMA_A11
- U200 pad A7: CRAMA_DQ6 -> CRAMA_A10
- U200 pad A8: CRAMA_DQ11 -> CRAMA_A9
- U200 pad A9: CRAMA_DQ12 -> CRAMA_ADVN
- U200 pad B1: CRAMB_DQ8 -> CRAMB_A2
- U200 pad B10: CRAMA_LBN -> CRAMA_CEN
- U200 pad B11: CRAMA_CEN -> CRAMA_A14
- U200 pad B12: CRAMA_WEN -> CRAMA_A8
- U200 pad B13: CRAMA_A0 -> CRAMA_A12
- U200 pad B14: CRAMA_A1 -> CRAMA_DQ13
- U200 pad B15: CRAMA_A3 -> CRAMA_DQ15
- U200 pad B2: CRAMB_DQ3 -> CRAMB_DQ2
- U200 pad B5: CRAMB_DQ10 -> CRAMB_DQ7
- U200 pad B9: CRAMA_UBN -> CRAMA_A7
- U200 pad C1: CRAMB_DQ7 -> CRAMB_CRE
- U200 pad C10: CRAMA_DQ15 -> CRAMA_A6
- U200 pad C13: CRAMA_A4 -> CRAMA_A5
- U200 pad C14: CRAMA_A5 -> CRAMA_A19
- U200 pad C15: CRAMA_A2 -> CRAMA_A18
- U200 pad C4: CRAMB_DQ14 -> CRAMB_WEN
- U200 pad C5: CRAMB_DQ9 -> CRAMB_CLK
- U200 pad C6: CRAMA_DQ1 -> CRAMA_DQ7
- U200 pad C7: CRAMA_DQ2 -> CRAMA_WEN
- U200 pad C8: CRAMA_DQ7 -> CRAMA_DQ6
- U200 pad C9: CRAMA_DQ8 -> CRAMA_DQ4
- U200 pad D1: CRAMB_DQ12 -> CRAMB_A0
- U200 pad D10: CRAMA_DQ14 -> CRAMA_DQ1
- U200 pad D11: CRAMA_DQ0 -> CRAMA_DQ2
- U200 pad D12: CRAMA_A6 -> CRAMA_UBN
- U200 pad D13: CRAMA_A7 -> CRAMA_A21
- U200 pad D15: CRAMA_A13 -> CRAMA_DQ14
- U200 pad D2: CRAMB_DQ11 -> CRAMB_A20
- U200 pad D3: CRAMB_OEN -> unconnected-(U200-PadD3)
- U200 pad D4: CRAMB_DQ13 -> CRAMB_ADVN
- U200 pad D7: CRAMA_DQ3 -> CRAMA_DQ0
- U200 pad D8: CRAMA_DQ4 -> CRAMA_DQ3
- U200 pad D9: CRAMA_DQ13 -> CRAMA_A16
- U200 pad E1: CRAMB_LBN -> CRAMB_A1
- U200 pad E11: CRAMA_A9 -> CRAMA_OEN
- U200 pad E12: CRAMA_A10 -> CRAMA_A3
- U200 pad E13: CRAMA_A11 -> CRAMA_A0
- U200 pad E14: CRAMA_A12 -> CRAMA_DQ11
- U200 pad E15: CRAMA_A17 -> CRAMA_DQ12
- U200 pad E2: CRAMB_DQ15 -> CRAMB_A11
- U200 pad E3: CRAMB_UBN -> CRAMB_A10
- U200 pad F1: CRAMB_WEN -> CRAMB_A4
- U200 pad F11: CRAMA_A8 -> CRAMA_A4
- U200 pad F14: CRAMA_A16 -> CRAMA_DQ8
- U200 pad F15: CRAMA_A15 -> CRAMA_DQ9
- U200 pad F3: CRAMB_WAIT -> CRAMB_DQ0
- U200 pad F4: CRAMB_CRE -> CRAMB_A9
- U200 pad G1: CRAMB_ADVN -> CRAMB_A7
- U200 pad G11: CRAMA_A20 -> CRAMA_CRE
- U200 pad G12: CRAMA_A21 -> CRAMA_A1
- U200 pad G13: CRAMA_A18 -> CRAMA_A2
- U200 pad G14: CRAMA_A19 -> CRAMA_DQ10
- U200 pad G15: CRAMA_A14 -> CRAMA_LBN
- U200 pad G4: CRAMB_DQ0 -> CRAMB_WAIT
- U200 pad H1: CRAMB_CLK -> CRAMB_A16
- U200 pad H2: CRAMB_A3 -> CRAMB_A17
- U200 pad H3: CRAMB_A1 -> CRAMB_A8
- U200 pad H4: CRAMB_A0 -> CRAMB_A18
- U200 pad J1: CRAMB_A7 -> CRAMB_A5
- U200 pad J2: CRAMB_A2 -> CRAMB_A3
- U200 pad J3: CRAMB_A5 -> CRAMB_A19
- U200 pad J4: CRAMB_A4 -> CRAMB_DQ15
- U200 pad K1: CRAMB_A6 -> CRAMB_A21
- U200 pad K14: unconnected-(U200-PadK14) -> SAI4_TX_BCLK
- U200 pad K2: CRAMB_A9 -> CRAMB_A6
- U200 pad K3: CRAMB_A8 -> unconnected-(U200-PadK3)
- U200 pad L1: CRAMB_A11 -> CRAMB_A13
- U200 pad L14: unconnected-(U200-PadL14) -> SAI4_TX_SYNC
- U200 pad L15: unconnected-(U200-PadL15) -> SAI4_TX_DATA
- U200 pad M1: CRAMB_A10 -> CRAMB_A15
- U200 pad M10: CSI_D1 -> CSI_D8
- U200 pad M13: unconnected-(U200-PadM13) -> UART2_RXD
- U200 pad M14: /fpga/K_UP -> /fpga/K_RIGHT
- U200 pad M2: CRAMB_A15 -> CRAMB_DQ14
- U200 pad M3: CRAMB_A13 -> CRAMB_A12
- U200 pad M4: CRAMB_A12 -> CRAMB_DQ13
- U200 pad M8: CSI_D13 -> CSI_D10
- U200 pad M9: CSI_D0 -> CSI_D6
- U200 pad N1: CRAMB_A19 -> CRAMB_DQ12
- U200 pad N10: CSI_D4 -> CSI_VSYNC
- U200 pad N11: CSI_D5 -> CSI_D15
- U200 pad N12: CSI_D2 -> CSI_D5
- U200 pad N13: unconnected-(U200-PadN13) -> UART2_TXD
- U200 pad N14: /fpga/K_RIGHT -> /fpga/K_SELECT
- U200 pad N15: /fpga/K_DOWN -> /fpga/K_UP
- U200 pad N2: CRAMB_A14 -> CRAMB_DQ11
- U200 pad N3: CRAMB_A17 -> CRAMB_A14
- U200 pad N7: CSI_D15 -> CSI_D11
- U200 pad P1: CRAMB_A18 -> CRAMB_DQ9
- U200 pad P10: CSI_D6 -> CSI_D13
- U200 pad P11: CSI_D7 -> CSI_D0
- U200 pad P12: CSI_D3 -> CSI_D4
- U200 pad P14: /fpga/K_START -> /fpga/K_A
- U200 pad P15: /fpga/K_SELECT -> /fpga/K_START
- U200 pad P2: unconnected-(U200-PadP2) -> CRAMB_DQ10
- U200 pad P3: CRAMB_A16 -> CRAMB_DQ8
- U200 pad P6: CSI_PCLK -> CSI_D9
- U200 pad P7: CSI_VSYNC -> CSI_D7
- U200 pad R10: CSI_D9 -> CSI_HSYNC
- U200 pad R11: CSI_D10 -> CSI_D3
- U200 pad R12: CSI_D11 -> CSI_D2
- U200 pad R13: /fpga/K_A -> /fpga/K_DOWN
- U200 pad R2: unconnected-(U200-PadR2) -> CRAMB_UBN
- U200 pad R3: CRAMB_A21 -> CRAMB_OEN
- U200 pad R4: CRAMB_A20 -> CRAMB_LBN
- U200 pad R5: CSI_HSYNC -> CSI_PCLK
- U200 pad R9: CSI_D8 -> CSI_D1
- U201 pad 15: /fpga/K_DOWN -> /fpga/K_UP
- U201 pad 18: /fpga/K_UP -> /fpga/K_DOWN
- U201 pad 2: KEY_UP -> KEY_DOWN
- U201 pad 5: KEY_DOWN -> KEY_UP
- U302 pad 2: CRAM_CEN -> CRAMA_CEN
- U802 pad B1: Net-(C824-Pad2) -> GND
- U802 pad B6: Net-(C835-Pad1) -> /usb/TYPEC_TX2N
- U802 pad C1: Net-(C823-Pad2) -> GND
- U802 pad C6: Net-(C836-Pad1) -> /usb/TYPEC_TX2P
- U802 pad D6: Net-(C834-Pad1) -> /usb/TYPEC_RX2P
- U802 pad E4: +1V8 -> +3V3
- U802 pad E6: Net-(C833-Pad1) -> /usb/TYPEC_RX2N
- U802 pad F6: Net-(C831-Pad1) -> /usb/TYPEC_TX1N
- U802 pad G6: Net-(C832-Pad1) -> /usb/TYPEC_TX1P
- U802 pad H1: Net-(C825-Pad2) -> GND
- U802 pad H3: +1V8 -> +3V3
- U802 pad H4: I2C1_SDA -> I2C3_SCL
- U802 pad H6: Net-(C830-Pad1) -> /usb/TYPEC_RX1P
- U802 pad J1: Net-(C826-Pad2) -> GND
- U802 pad J4: I2C1_SCL -> I2C3_SDA
- U802 pad J5: +1V8 -> +3V3
- U802 pad J6: Net-(C829-Pad1) -> /usb/TYPEC_RX1N
- U803 pad J7: Net-(C823-Pad1) -> unconnected-(U803-PadJ7)
- U803 pad J9: Net-(C825-Pad1) -> unconnected-(U803-PadJ9)
- U803 pad K7: Net-(C824-Pad1) -> unconnected-(U803-PadK7)
- U803 pad K9: Net-(C826-Pad1) -> unconnected-(U803-PadK9)
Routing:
- net GND: track 0.00 -> 160.6 mm, vias 0 -> 76
- net I2C1_SCL: track 0.00 -> 102.6 mm, vias 0 -> 4
- net I2C1_SDA: track 0.00 -> 97.8 mm, vias 0 -> 4
- net I2C3_SCL: track 0.00 -> 78.1 mm, vias 0 -> 6
- net UART2_TXD: track 0.00 -> 78.0 mm, vias 0 -> 5
- net I2C3_SDA: track 0.00 -> 77.1 mm, vias 0 -> 6
- net UART2_RXD: track 0.00 -> 71.3 mm, vias 0 -> 4
- net /fpga/FPGA_TDO: track 0.00 -> 65.4 mm, vias 0 -> 3
- net /fpga/FPGA_TCK: track 0.00 -> 64.3 mm, vias 0 -> 3
- net /fpga/FPGA_TMS: track 0.00 -> 63.5 mm, vias 0 -> 3
- net FSPI_2A_SCK: track 0.00 -> 61.0 mm, vias 0 -> 4
- net PMU_IRQ: track 0.00 -> 61.0 mm, vias 0 -> 3
- net /fpga/FPGA_TDI: track 0.00 -> 59.9 mm, vias 0 -> 3
- net I2C4_SDA: track 0.00 -> 58.4 mm, vias 0 -> 5
- net I2C4_SCL: track 0.00 -> 56.6 mm, vias 0 -> 5
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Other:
- copper layers 4 -> 6
- board text added: "Fobu r0.3"
